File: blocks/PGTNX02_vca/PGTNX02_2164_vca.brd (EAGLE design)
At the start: 45.6 x 69.8 mm, 77 parts, among them IC3 TL074P

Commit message: 2164 vca board layout + rotary encoder breakout pcb
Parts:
- removed BIAS1, BIAS2, BIAS3: HEADER/MALE/01, connectors:HEADER/MALE/01
- added BIA1, BIA2, BIA3, BIB1, BIB2, BIB3: HEADER/MALE/01, connectors:HEADER/MALE/01
- IC1: value (none) -> 79L05
- IC2: value (none) -> V2164
- R14: value 100k -> 300k; device resistors:TRIMMER/64B -> resistors:RESISTOR/7.5
- moved C15 302.9 mm to (8.89, 59.7), turned to 90 degrees
- moved IC1 297.0 mm to (14.0, 58.4), turned to 270 degrees
- moved SWLB2 282.3 mm to (1.27, 53.3), turned to 180 degrees
- moved SWEB2 269.6 mm to (1.27, 48.3), turned to 180 degrees
- moved SWLA2 268.3 mm to (1.27, 43.2), turned to 180 degrees
- moved D1 266.7 mm to (27.9, 33.0)
- moved SWCB2 264.5 mm to (1.27, 50.8), turned to 180 degrees
- moved R21 259.9 mm to (33.0, 7.62)
- moved SWEA2 255.7 mm to (1.27, 38.1), turned to 180 degrees
- moved SWCA2 250.6 mm to (1.27, 40.6), turned to 180 degrees
- moved SWEB1 244.4 mm to (3.81, 48.3)
- moved SWCB1 243.1 mm to (3.81, 50.8)
- moved SWLB1 241.9 mm to (3.81, 53.3)
- moved R20 227.6 mm to (17.8, 20.3), turned to 180 degrees
- moved SWEA1 222.9 mm to (3.81, 38.1)
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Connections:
- new net N$33: BIB1.1, R14.2
- new net N$34: BIA2.1, SWEA2.1
- net +12V: now also R14.1
- net N$21: now also BIB2.1; no longer BIAS2.1, R14.2, SWEA2.1
- net N$31: now also BIA1.1; no longer BIAS1.1, R14.3
- net PE: now also BIA3.1, BIB3.1; no longer BIAS3.1, R14.1
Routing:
- net +12V: track 0.00 -> 96.0 mm, vias 0 -> 1
- net -12V: track 0.00 -> 81.6 mm
- net N$16: track 0.00 -> 64.9 mm
- net N$20: track 0.00 -> 58.8 mm
- net N$34: track 0.00 -> 57.3 mm, vias 0 -> 2
- net N$21: track 0.00 -> 55.8 mm, vias 0 -> 1
- net N$18: track 0.00 -> 54.6 mm
- net N$10: track 0.00 -> 53.1 mm
- net N$26: track 0.00 -> 52.7 mm
- net -5V: track 0.00 -> 50.1 mm
- net N$29: track 0.00 -> 44.7 mm, vias 0 -> 1
- net N$30: track 0.00 -> 42.6 mm
- net N$6: track 0.00 -> 40.7 mm
- net N$15: track 0.00 -> 35.1 mm
- net N$27: track 0.00 -> 30.0 mm, vias 0 -> 2
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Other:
- board text added: "2164_VCA"
- board text removed: "VC AMPLIFIER"

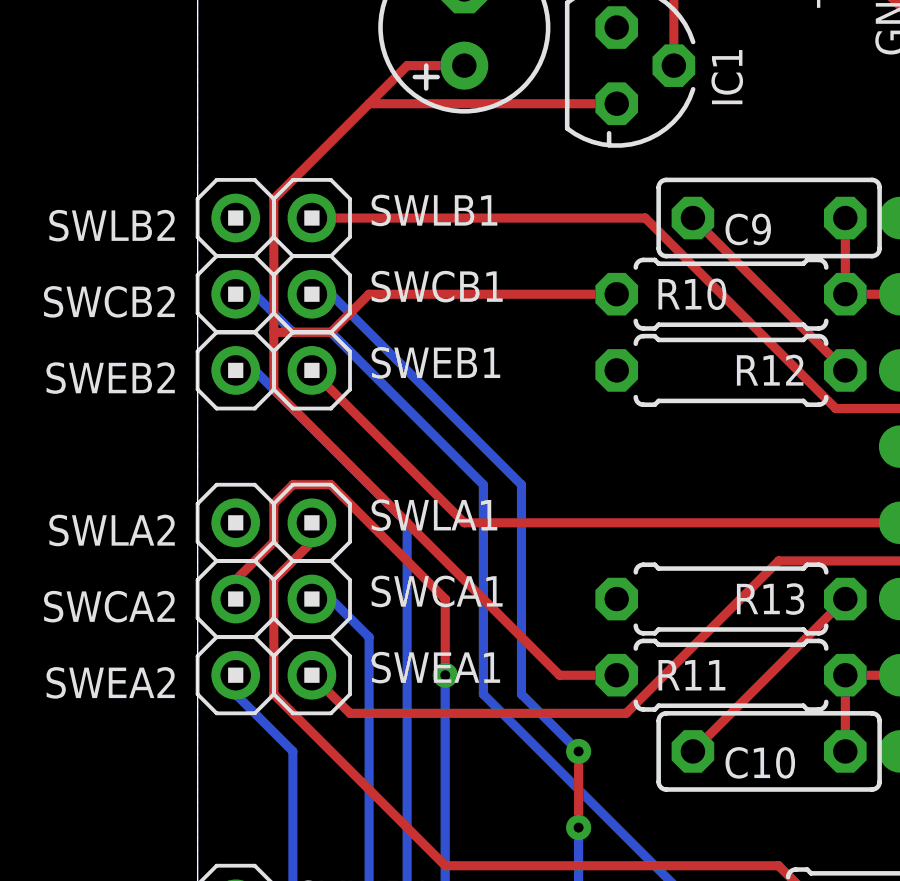
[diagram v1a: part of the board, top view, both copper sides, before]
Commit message: Added error history to VCA, corrected some label errors and changed a resistor value.
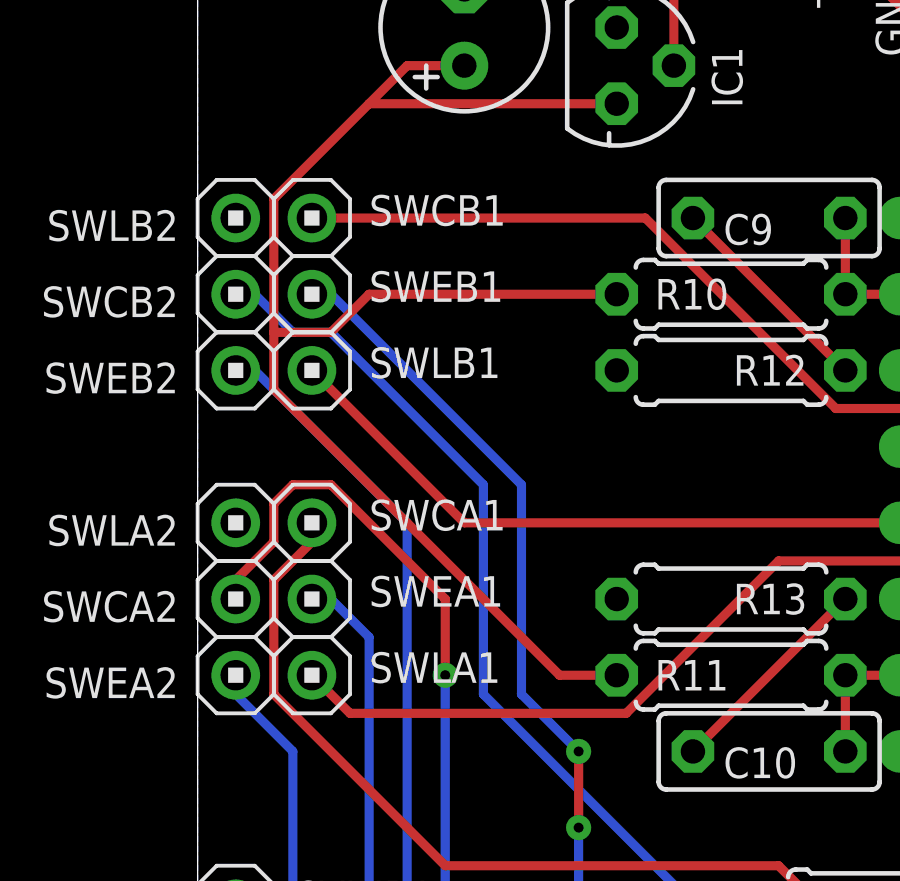
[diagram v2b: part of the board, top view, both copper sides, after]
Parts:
- R12, R13, R4, R6: value 500R -> 510R
- moved SWLB1 5.08 mm to (3.81, 48.3)
- moved SWLA1 5.08 mm to (3.81, 38.1)
- moved SWCB1 2.54 mm to (3.81, 53.3)
- moved SWCA1 2.54 mm to (3.81, 43.2)
- moved SWEA1 2.54 mm to (3.81, 40.6)
- moved SWEB1 2.54 mm to (3.81, 50.8)
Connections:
- net N$15: now also SWEA1.1; no longer SWCA1.1
- net N$16: now also SWCA1.1; no longer SWLA1.1
- net N$19: now also SWLA1.1; no longer SWEA1.1
- net N$26: now also SWCB1.1; no longer SWLB1.1
- net N$27: now also SWEB1.1; no longer SWCB1.1
- net N$28: now also SWLB1.1; no longer SWEB1.1
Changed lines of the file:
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@@
 <attribute name="VALUE" x="33.401" y="50.546" size="1.27" layer="27" ratio="10"/>
 </element>
-<element name="R4" library="resistors" package="RESISTOR/7.5" value="500R" x="41.91" y="57.15" smashed="yes" rot="R270">
+<element name="R4" library="resistors" package="RESISTOR/7.5" value="510R" x="41.91" y="57.15" smashed="yes" rot="R270">
 <attribute name="NAME" x="41.402" y="59.69" size="1.016" layer="25" ratio="10" rot="R270"/>
 <attribute name="VALUE" x="43.2562" y="60.071" size="1.27" layer="27" ratio="10" rot="R270"/>
@@
 <attribute name="VALUE" x="33.401" y="32.766" size="1.27" layer="27" ratio="10"/>
 </element>
-<element name="R6" library="resistors" package="RESISTOR/7.5" value="500R" x="41.91" y="31.75" smashed="yes" rot="R90">
+<element name="R6" library="resistors" package="RESISTOR/7.5" value="510R" x="41.91" y="31.75" smashed="yes" rot="R90">
 <attribute name="NAME" x="42.418" y="29.21" size="1.016" layer="25" ratio="10" rot="R90"/>
 <attribute name="VALUE" x="40.5638" y="28.829" size="1.27" layer="27" ratio="10" rot="R90"/>
@@
 <attribute name="VALUE" x="15.621" y="50.546" size="1.27" layer="27" ratio="10"/>
 </element>
-<element name="R12" library="resistors" package="RESISTOR/7.5" value="500R" x="17.78" y="48.26" smashed="yes" rot="R180">
+<element name="R12" library="resistors" package="RESISTOR/7.5" value="510R" x="17.78" y="48.26" smashed="yes" rot="R180">
 <attribute name="NAME" x="20.32" y="48.768" size="1.016" layer="25" ratio="10" rot="R180"/>
 <attribute name="VALUE" x="20.701" y="46.9138" size="1.27" layer="27" ratio="10" rot="R180"/>
@@
 <attribute name="VALUE" x="15.621" y="32.766" size="1.27" layer="27" ratio="10"/>
 </element>
-<element name="R13" library="resistors" package="RESISTOR/7.5" value="500R" x="17.78" y="40.64" smashed="yes" rot="R180">
+<element name="R13" library="resistors" package="RESISTOR/7.5" value="510R" x="17.78" y="40.64" smashed="yes" rot="R180">
 <attribute name="NAME" x="20.32" y="41.148" size="1.016" layer="25" ratio="10" rot="R180"/>
 <attribute name="VALUE" x="20.701" y="39.2938" size="1.27" layer="27" ratio="10" rot="R180"/>
@@
 <attribute name="VALUE" x="40.259" y="18.034" size="1.27" layer="27" ratio="10" rot="R180"/>
 </element>
-<element name="SWLA1" library="connectors" package="HEADER/MALE/01" value="HEADER/MALE/01" x="3.81" y="43.18" smashed="yes">
+<element name="SWCA1" library="connectors" package="HEADER/MALE/01" value="HEADER/MALE/01" x="3.81" y="43.18" smashed="yes">
 <attribute name="NAME" x="5.715" y="42.926" size="1.016" layer="25" ratio="10"/>
 </element>
-<element name="SWCA1" library="connectors" package="HEADER/MALE/01" value="HEADER/MALE/01" x="3.81" y="40.64" smashed="yes">
+<element name="SWEA1" library="connectors" package="HEADER/MALE/01" value="HEADER/MALE/01" x="3.81" y="40.64" smashed="yes">
 <attribute name="NAME" x="5.715" y="40.386" size="1.016" layer="25" ratio="10"/>
 </element>
-<element name="SWEA1" library="connectors" package="HEADER/MALE/01" value="HEADER/MALE/01" x="3.81" y="38.1" smashed="yes">
+<element name="SWLA1" library="connectors" package="HEADER/MALE/01" value="HEADER/MALE/01" x="3.81" y="38.1" smashed="yes">
 <attribute name="NAME" x="5.715" y="37.846" size="1.016" layer="25" ratio="10"/>
 </element>
-<element name="SWLB1" library="connectors" package="HEADER/MALE/01" value="HEADER/MALE/01" x="3.81" y="53.34" smashed="yes">
+<element name="SWCB1" library="connectors" package="HEADER/MALE/01" value="HEADER/MALE/01" x="3.81" y="53.34" smashed="yes">
 <attribute name="NAME" x="5.715" y="53.086" size="1.016" layer="25" ratio="10"/>
 </element>
-<element name="SWCB1" library="connectors" package="HEADER/MALE/01" value="HEADER/MALE/01" x="3.81" y="50.8" smashed="yes">
+<element name="SWEB1" library="connectors" package="HEADER/MALE/01" value="HEADER/MALE/01" x="3.81" y="50.8" smashed="yes">
 <attribute name="NAME" x="5.715" y="50.546" size="1.016" layer="25" ratio="10"/>
 </element>
-<element name="SWEB1" library="connectors" package="HEADER/MALE/01" value="HEADER/MALE/01" x="3.81" y="48.26" smashed="yes">
+<element name="SWLB1" library="connectors" package="HEADER/MALE/01" value="HEADER/MALE/01" x="3.81" y="48.26" smashed="yes">
 <attribute name="NAME" x="5.715" y="48.006" size="1.016" layer="25" ratio="10"/>
 </element>
@@
 <contactref element="C12" pad="1"/>
 <contactref element="IC3" pad="2"/>
-<contactref element="SWLB1" pad="1"/>
+<contactref element="SWCB1" pad="1"/>
 <wire x1="24.13" y1="22.86" x2="21.59" y2="22.86" width="0.3048" layer="1"/>
 <wire x1="26.67" y1="30.48" x2="26.67" y2="27.94" width="0.3048" layer="1"/>
@@
 <signal name="N$15">
 <contactref element="R1" pad="1"/>
-<contactref element="SWCA1" pad="1"/>
+<contactref element="SWEA1" pad="1"/>
 <wire x1="5.715" y1="18.415" x2="13.97" y2="10.16" width="0.3048" layer="16"/>
 <wire x1="5.715" y1="39.37" x2="5.715" y2="18.415" width="0.3048" layer="16"/>
@@
 <signal name="N$16">
 <contactref element="C11" pad="1"/>
-<contactref element="SWLA1" pad="1"/>
+<contactref element="SWCA1" pad="1"/>
 <contactref element="IC3" pad="6"/>
 <contactref element="R16" pad="2"/>
@@
 <signal name="N$19">
 <contactref element="IC2" pad="4"/>
-<contactref element="SWEA1" pad="1"/>
+<contactref element="SWLA1" pad="1"/>
 <wire x1="26.035" y1="43.815" x2="24.13" y2="45.72" width="0.3048" layer="1"/>
 <wire x1="26.035" y1="42.545" x2="26.035" y2="43.815" width="0.3048" layer="1"/>
@@
 <signal name="N$27">
 <contactref element="R9" pad="1"/>
-<contactref element="SWCB1" pad="1"/>
+<contactref element="SWEB1" pad="1"/>
 <wire x1="12.7" y1="26.67" x2="13.97" y2="25.4" width="0.3048" layer="16"/>
 <wire x1="12.7" y1="33.02" x2="12.7" y2="26.67" width="0.3048" layer="16"/>
@@
 </signal>
 <signal name="N$28">
-<contactref element="SWEB1" pad="1"/>
+<contactref element="SWLB1" pad="1"/>
 <contactref element="IC2" pad="5"/>
 <wire x1="8.89" y1="43.18" x2="24.13" y2="43.18" width="0.3048" layer="1"/>

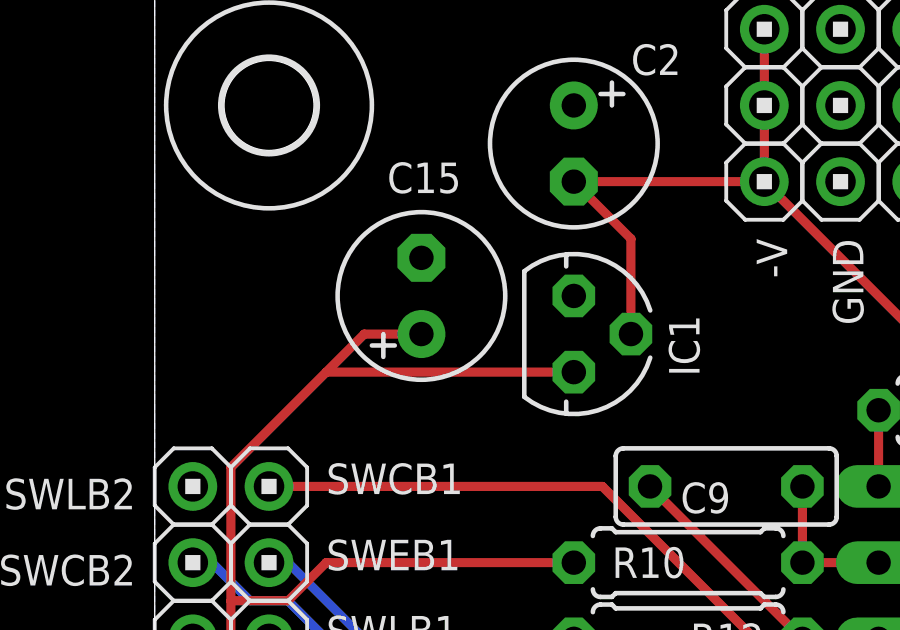
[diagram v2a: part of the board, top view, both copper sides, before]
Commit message: Corrected Polarity of C15
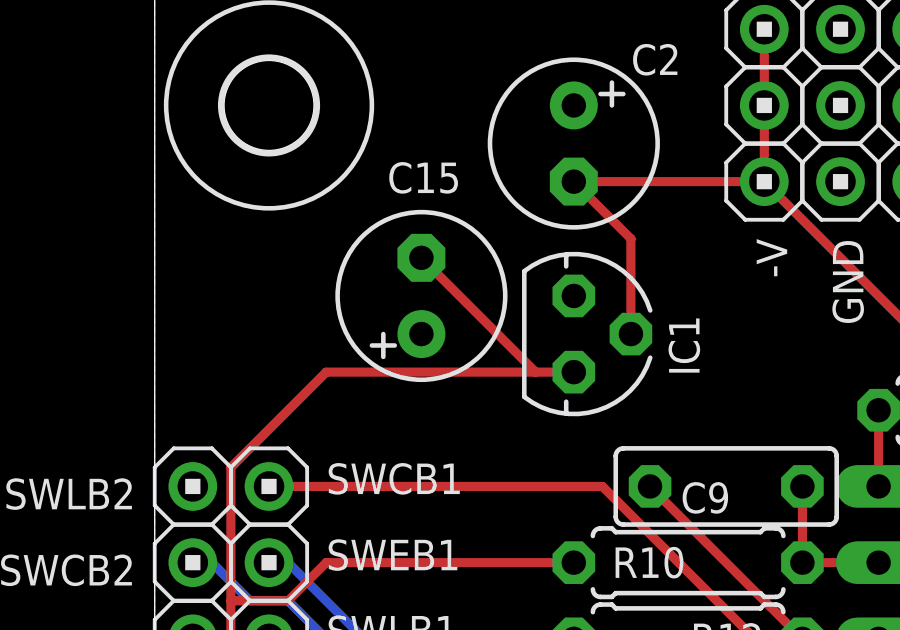
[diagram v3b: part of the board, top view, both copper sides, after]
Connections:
- net -5V: now also C15.-; no longer C15.+
- net PE: now also C15.+; no longer C15.-
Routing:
- net -5V: track 50.1 -> 51.8 mm
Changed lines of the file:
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@@
 <contactref element="IC2" pad="8"/>
 <contactref element="D1" pad="C"/>
-<contactref element="C15" pad="-"/>
 <contactref element="IC1" pad="GND"/>
 <contactref element="BIA3" pad="1"/>
 <contactref element="BIB3" pad="1"/>
+<contactref element="C15" pad="+"/>
 </signal>
 <signal name="+12V">
@@
 <contactref element="R11" pad="1"/>
 <contactref element="IC1" pad="OUT"/>
-<contactref element="C15" pad="+"/>
 <wire x1="12.065" y1="38.1" x2="13.97" y2="38.1" width="0.3048" layer="1"/>
 <wire x1="2.54" y1="47.625" x2="12.065" y2="38.1" width="0.3048" layer="1"/>
 <wire x1="2.54" y1="53.975" x2="2.54" y2="49.53" width="0.3048" layer="1"/>
 <wire x1="2.54" y1="49.53" x2="2.54" y2="47.625" width="0.3048" layer="1"/>
-<wire x1="6.985" y1="58.42" x2="5.715" y2="57.15" width="0.3048" layer="1"/>
 <wire x1="5.715" y1="57.15" x2="2.54" y2="53.975" width="0.3048" layer="1"/>
-<wire x1="8.89" y1="58.42" x2="6.985" y2="58.42" width="0.3048" layer="1"/>
 <wire x1="5.715" y1="50.8" x2="13.97" y2="50.8" width="0.3048" layer="1"/>
 <wire x1="4.445" y1="49.53" x2="5.715" y2="50.8" width="0.3048" layer="1"/>
 <wire x1="2.54" y1="49.53" x2="4.445" y2="49.53" width="0.3048" layer="1"/>
-<wire x1="5.715" y1="57.15" x2="13.97" y2="57.15" width="0.3048" layer="1"/>
+<wire x1="5.715" y1="57.15" x2="12.7" y2="57.15" width="0.3048" layer="1"/>
+<contactref element="C15" pad="-"/>
+<wire x1="12.7" y1="57.15" x2="13.97" y2="57.15" width="0.3048" layer="1"/>
+<wire x1="12.7" y1="57.15" x2="8.89" y2="60.96" width="0.3048" layer="1"/>
 </signal>
 <signal name="N$20">

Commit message: Changes
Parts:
- moved SWLB1 5.08 mm to (3.81, 53.3)
- moved SWLA1 5.08 mm to (3.81, 43.2)
- moved SWCB1 2.54 mm to (3.81, 50.8)
- moved SWCA1 2.54 mm to (3.81, 40.6)
- moved SWEA1 2.54 mm to (3.81, 38.1)
- moved SWEB1 2.54 mm to (3.81, 48.3)
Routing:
- net +12V: track 96.0 -> 0.00 mm, vias 1 -> 0
- net -12V: track 81.6 -> 0.00 mm
- net N$16: track 64.9 -> 0.00 mm
- net N$20: track 58.8 -> 0.00 mm
- net N$34: track 57.3 -> 0.00 mm, vias 2 -> 0
- net N$21: track 55.8 -> 0.00 mm, vias 1 -> 0
- net N$18: track 54.6 -> 0.00 mm
- net N$10: track 53.1 -> 0.00 mm
- net N$26: track 52.7 -> 0.00 mm
- net -5V: track 51.8 -> 0.00 mm
- net N$29: track 44.7 -> 0.00 mm, vias 1 -> 0
- net N$30: track 42.6 -> 0.00 mm
- net N$6: track 40.7 -> 0.00 mm
- net N$15: track 35.1 -> 0.00 mm
- net N$27: track 30.0 -> 0.00 mm, vias 2 -> 0
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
